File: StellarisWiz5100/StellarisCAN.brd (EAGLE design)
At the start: 86 x 84.4 mm, 10 parts

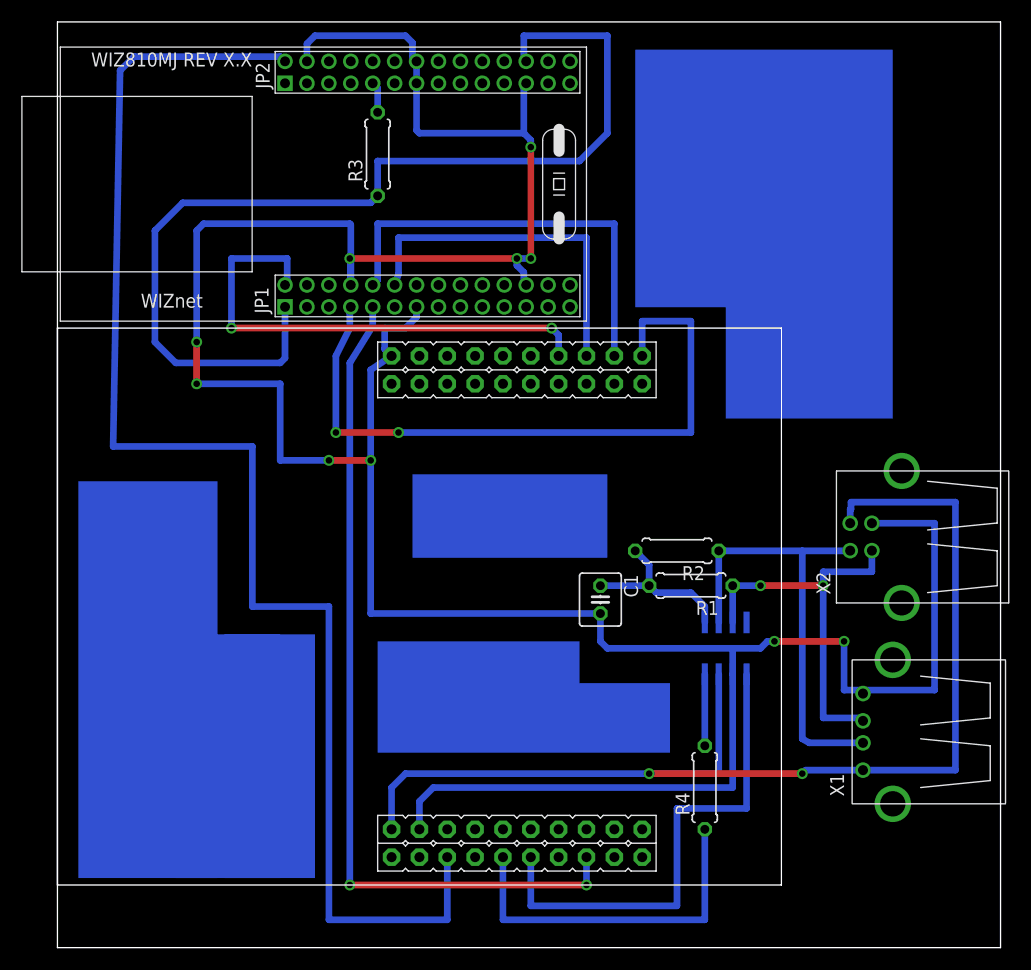
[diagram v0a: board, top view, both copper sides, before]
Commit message: 
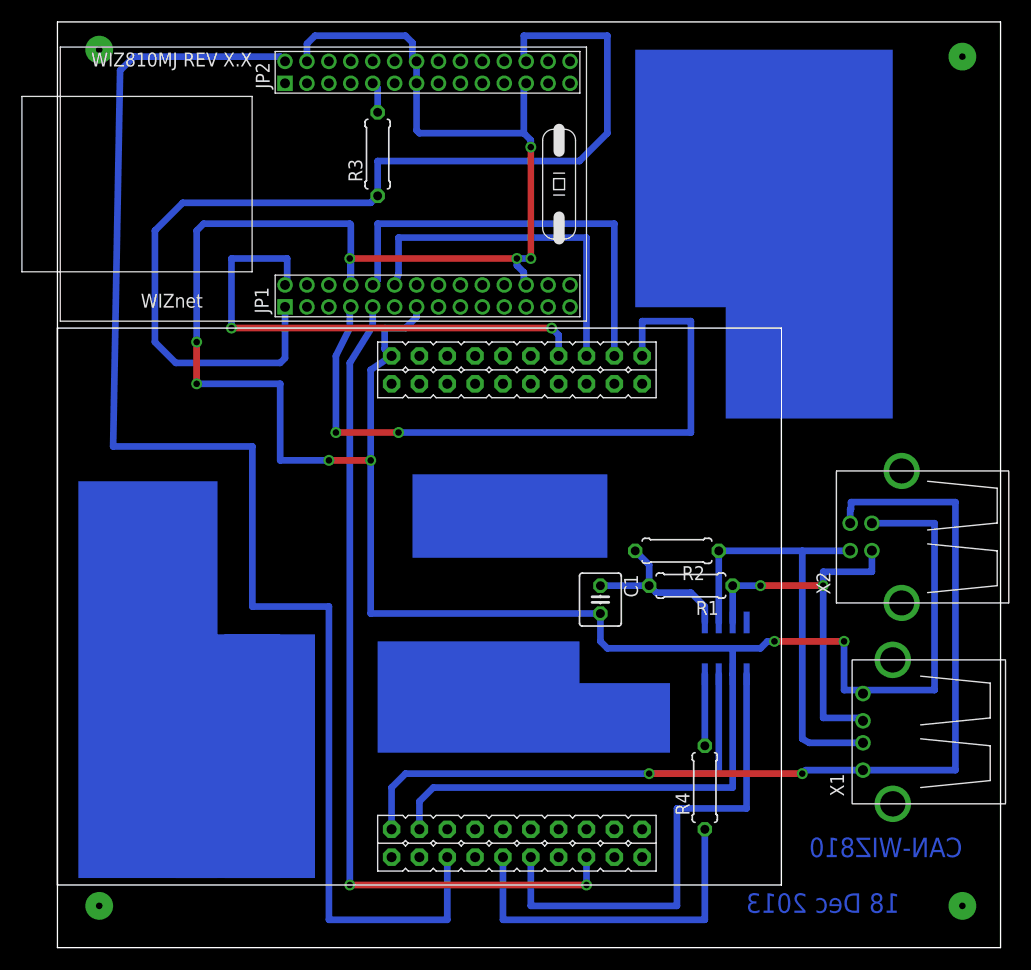
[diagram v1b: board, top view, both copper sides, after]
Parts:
- C1: value (none) -> 47n
- R3: value (none) -> 1K
- R4: value 60 -> 1k
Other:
- board text added: "18 Dec 2013"
- board text added: "CAN-WIZ810"
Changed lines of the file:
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@@
 <layer number="27" name="tValues" color="7" fill="1" visible="yes" active="yes"/>
 <layer number="28" name="bValues" color="7" fill="1" visible="yes" active="yes"/>
-<layer number="29" name="tStop" color="7" fill="3" visible="no" active="yes"/>
-<layer number="30" name="bStop" color="7" fill="6" visible="no" active="yes"/>
-<layer number="31" name="tCream" color="7" fill="4" visible="no" active="yes"/>
-<layer number="32" name="bCream" color="7" fill="5" visible="no" active="yes"/>
-<layer number="33" name="tFinish" color="6" fill="3" visible="no" active="yes"/>
-<layer number="34" name="bFinish" color="6" fill="6" visible="no" active="yes"/>
-<layer number="35" name="tGlue" color="7" fill="4" visible="no" active="yes"/>
-<layer number="36" name="bGlue" color="7" fill="5" visible="no" active="yes"/>
-<layer number="37" name="tTest" color="7" fill="1" visible="no" active="yes"/>
-<layer number="38" name="bTest" color="7" fill="1" visible="no" active="yes"/>
+<layer number="29" name="tStop" color="7" fill="3" visible="yes" active="yes"/>
+<layer number="30" name="bStop" color="7" fill="6" visible="yes" active="yes"/>
+<layer number="31" name="tCream" color="7" fill="4" visible="yes" active="yes"/>
+<layer number="32" name="bCream" color="7" fill="5" visible="yes" active="yes"/>
+<layer number="33" name="tFinish" color="6" fill="3" visible="yes" active="yes"/>
+<layer number="34" name="bFinish" color="6" fill="6" visible="yes" active="yes"/>
+<layer number="35" name="tGlue" color="7" fill="4" visible="yes" active="yes"/>
+<layer number="36" name="bGlue" color="7" fill="5" visible="yes" active="yes"/>
+<layer number="37" name="tTest" color="7" fill="1" visible="yes" active="yes"/>
+<layer number="38" name="bTest" color="7" fill="1" visible="yes" active="yes"/>
 <layer number="39" name="tKeepout" color="4" fill="11" visible="yes" active="yes"/>
 <layer number="40" name="bKeepout" color="1" fill="11" visible="yes" active="yes"/>
@@
 <layer number="42" name="bRestrict" color="1" fill="10" visible="yes" active="yes"/>
 <layer number="43" name="vRestrict" color="2" fill="10" visible="yes" active="yes"/>
-<layer number="44" name="Drills" color="7" fill="1" visible="no" active="yes"/>
-<layer number="45" name="Holes" color="7" fill="1" visible="no" active="yes"/>
-<layer number="46" name="Milling" color="3" fill="1" visible="no" active="yes"/>
-<layer number="47" name="Measures" color="7" fill="1" visible="no" active="yes"/>
+<layer number="44" name="Drills" color="7" fill="1" visible="yes" active="yes"/>
+<layer number="45" name="Holes" color="7" fill="1" visible="yes" active="yes"/>
+<layer number="46" name="Milling" color="3" fill="1" visible="yes" active="yes"/>
+<layer number="47" name="Measures" color="7" fill="1" visible="yes" active="yes"/>
 <layer number="48" name="Document" color="7" fill="1" visible="yes" active="yes"/>
 <layer number="49" name="Reference" color="7" fill="1" visible="yes" active="yes"/>
@@
 <layer number="132" name="bAdjust" color="7" fill="1" visible="yes" active="yes"/>
 <layer number="144" name="Drill_legend" color="7" fill="1" visible="yes" active="yes"/>
-<layer number="150" name="Notes" color="7" fill="1" visible="no" active="yes"/>
+<layer number="150" name="Notes" color="7" fill="1" visible="yes" active="yes"/>
 <layer number="151" name="HeatSink" color="7" fill="1" visible="yes" active="yes"/>
 <layer number="152" name="_bDocu" color="7" fill="1" visible="yes" active="yes"/>
@@
 <rectangle x1="29.21" y1="17.78" x2="47.625" y2="27.94" layer="16"/>
 <rectangle x1="47.625" y1="17.78" x2="55.88" y2="24.13" layer="16"/>
+<text x="82.55" y="8.255" size="1.778" layer="16" rot="MR0">CAN-WIZ810</text>
+<text x="76.835" y="3.175" size="1.778" layer="16" rot="MR0">18 Dec 2013</text>
 </plain>
 <attributes>
@@
 <element name="U$2" library="WIZNET" package="WIZ810MJ" value="WIZ810MJ" x="48.26" y="57.15" rot="R180"/>
 <element name="U$1" library="lieven" package="LAUNCHPAD-XL" value="STELLARIS-LAUNCHPADSTELLARIS-LAUNCHPAD-XL" x="0" y="5.715"/>
-<element name="R3" library="rcl" package="0207/7" value="" x="29.21" y="72.39" rot="R90"/>
+<element name="R3" library="rcl" package="0207/7" value="1K" x="29.21" y="72.39" rot="R90"/>
 <element name="U$3" library="lieven" package="SOIC8-N_MC" value="TJA1040" x="60.96" y="27.305" rot="MR90"/>
 <element name="X1" library="lieven" package="USB-A-H" value="" x="76.2" y="19.685" rot="R180"/>
 <element name="R1" library="rcl" package="0207/7" value="60" x="57.785" y="33.02" rot="R180"/>
 <element name="R2" library="rcl" package="0207/7" value="60" x="56.515" y="36.195" rot="R180"/>
-<element name="C1" library="rcl" package="C025-040X050" value="" x="49.53" y="31.75" rot="R270"/>
+<element name="C1" library="rcl" package="C025-040X050" value="47n" x="49.53" y="31.75" rot="R270"/>
 <element name="X2" library="lieven" package="USB-B-H" value="" x="74.295" y="37.465" rot="R180"/>
-<element name="R4" library="rcl" package="0207/7" value="60" x="59.055" y="14.605" rot="R90"/>
+<element name="R4" library="rcl" package="0207/7" value="1k" x="59.055" y="14.605" rot="R90"/>
 </elements>
 <signals>
@@
 <wire x1="20.955" y1="60.645" x2="20.76" y2="60.45" width="0.6096" layer="16"/>
 </signal>
+<signal name="N$14">
+<via x="3.81" y="3.81" extent="1-16" drill="0.6" diameter="2.54"/>
+</signal>
+<signal name="N$15">
+<via x="82.55" y="3.81" extent="1-16" drill="0.6" diameter="2.54"/>
+</signal>
+<signal name="N$16">
+<via x="82.55" y="81.28" extent="1-16" drill="0.6" diameter="2.54"/>
+</signal>
+<signal name="N$17">
+<via x="3.81" y="81.915" extent="1-16" drill="0.6" diameter="2.54"/>
+</signal>
 </signals>
